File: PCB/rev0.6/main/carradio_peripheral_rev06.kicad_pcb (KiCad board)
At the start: 4 copper layers, 100 x 100 mm, 213 parts, among them J1 ISO 10487 A (via pigtail), J10 K-line module socket, J12 Display buttons, J13 HDMI in (from VIM3), J14 Display FPC 40P 0.5mm, J18 VIM3 VIN (JST-XH 2P), J2 VIM3 40-pin via 2x20 IDC ribb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, J21 Expansion 2, J22 SWD, J23 Audio module socket, J25 USB module socket, J27 GNSS module socket, J5 VIM3 POWER key lead, J7 BH1750 light sensor, J8 ISO 10487 C1 (via pigtail), Q1 AO3400A, Q10 P-MOSFET -40V, Q11 CSD18543Q3A, Q12 CSD18543Q3A, Q2 P-MOSFET -60V, Q3 2N7002, SW1 BOOTSEL, SW2 RESET, U1 TPS560430XDBVR, U12 TPS55288RPMR, U13 CH334R, U19 AP2112K-3.3, U2 EL817S1(C), U20 RP2350B, U21 W25Q128JVS, U3 EL817S1(C), U4 EL817S1(C), U5 EL817S1(C), U6 LP5907MFX-3.3, Y1 12MHz, Y3 12MHz

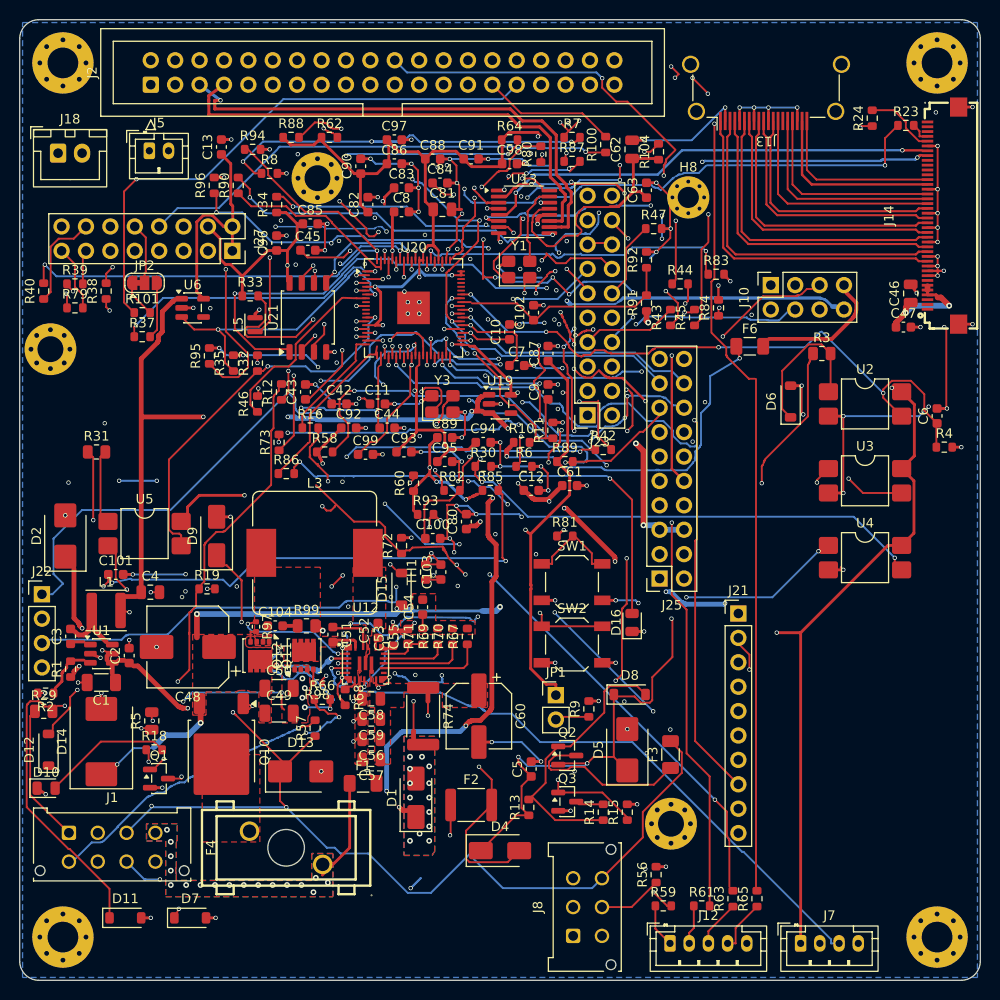
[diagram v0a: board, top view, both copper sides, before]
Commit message: PCB rev 0.6: larger via pads where possible, join traces to nearby vias
- viaup.py: via pads grow to 0.60/0.55/0.50 mm where they still clear
  other-net copper by 0.15 mm (355 vias), for a larger annular ring
  around the 0.3 mm holes; vias under the RP2350B stay 0.45 mm so the
  exposed-pad GND pour keeps its connection.
- viajoin.py: 31 same-net traces that passed within 0.18 mm of a via
  hole without touching are joined to the via (JLC "PTH to trace").
- Order files and DFM notes updated.

DRC: 0 unconnected, no errors; schematic parity unchanged.

Co-Authored-By: Claude Opus 5.5 (1M context) <noreply@anthropic.com>
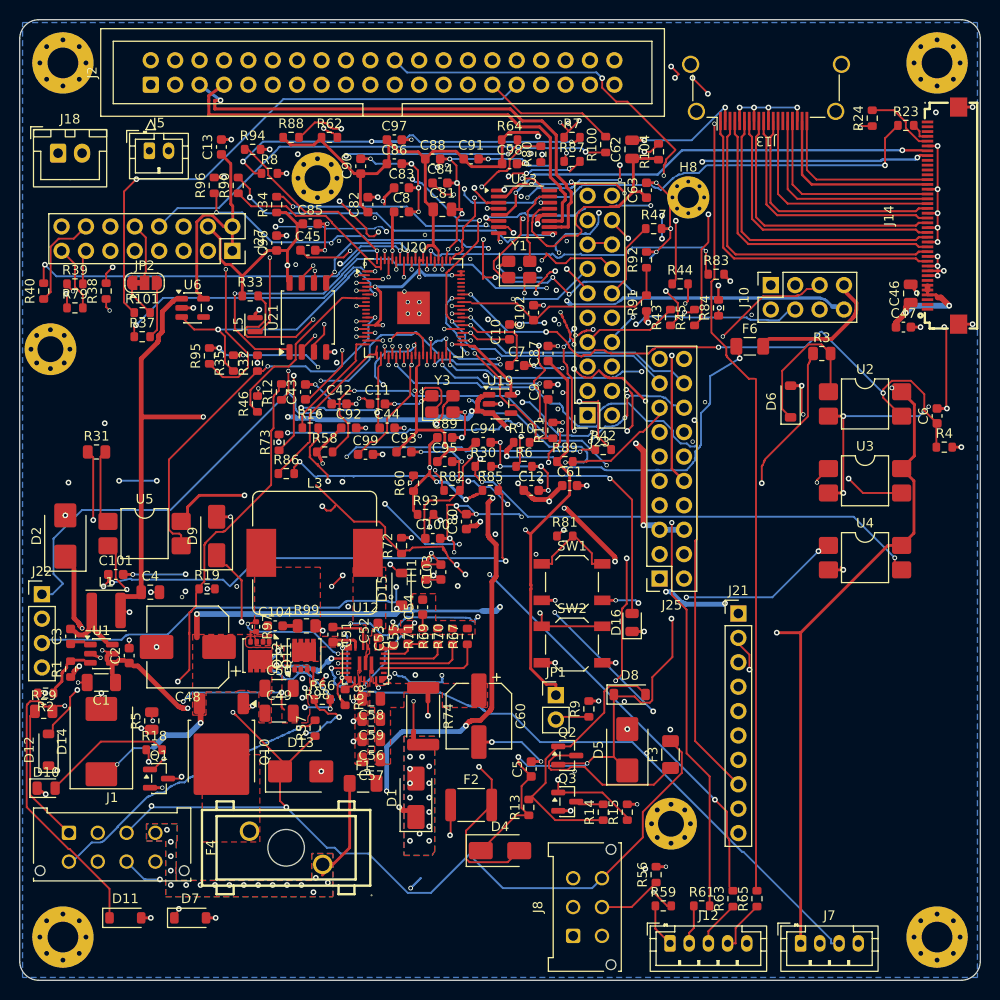
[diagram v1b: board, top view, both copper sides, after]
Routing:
- net /VBAT_P: track 128.4 -> 130.5 mm
- net GND: track 660.6 -> 662.6 mm
- net /MCU_RUN: track 100.8 -> 101.6 mm
- net /VIM3_PWR_EN: track 89.7 -> 90.5 mm
- net /+5V_AON: track 180.6 -> 181.1 mm

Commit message: PCB rev 0.6: VIM3 power key through a PhotoMOS (U22, AQY210S)
U22 shorts the two J5 pins (the VIM3 POWER key pads), isolated, instead of
Q1 pulling J5 pin 1 to GND. It sits on the bottom side next to J5; R12 is
now the 390 ohm LED resistor from GPIO15, R19 is gone. Schematic, board,
order files, LCSC list and docs updated. DRC: 0 unconnected, no errors.
bridge.py vias now use the board's 0.3 mm drill. A stale KiCad lock file is
untracked and *.lck ignored.

Co-Authored-By: Claude Opus 5.5 (1M context) <noreply@anthropic.com>
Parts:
- removed Q1: AO3400A, Package_TO_SOT_SMD:SOT-23
- removed R19: 100k, Resistor_SMD:R_0603_1608Metric
- added U22: AQY210S, Package_SO:SO-4_4.4x4.3mm_P2.54mm, B.Cu at (19.2, 15.0)
- R12: value 100Ω -> 390Ω
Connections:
- J5 pad 1: /VIM3_PWR_KEY -> /VIM3_PWR_KEY_A
- J5 pad 2: GND -> /VIM3_PWR_KEY_B
- R12 pad 2: /PWR_KEY_G -> /PWR_KEY_LED
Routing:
- net /VIM3_PWR_KEY: track 70.5 -> 0.00 mm, vias 1 -> 0
- net /PWR_KEY_G: track 43.8 -> 0.00 mm, vias 2 -> 0
- net /PWR_KEY_LED: track 0.00 -> 21.7 mm, vias 0 -> 2
- net /VIM3_PWR_KEY_B: track 0.00 -> 4.27 mm
- net /VIM3_PWR_KEY_A: track 0.00 -> 3.64 mm
- net GND: track 662.6 -> 660.5 mm
